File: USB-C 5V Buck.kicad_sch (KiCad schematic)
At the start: 10 parts, among them U8 TPSM365R3RDNR

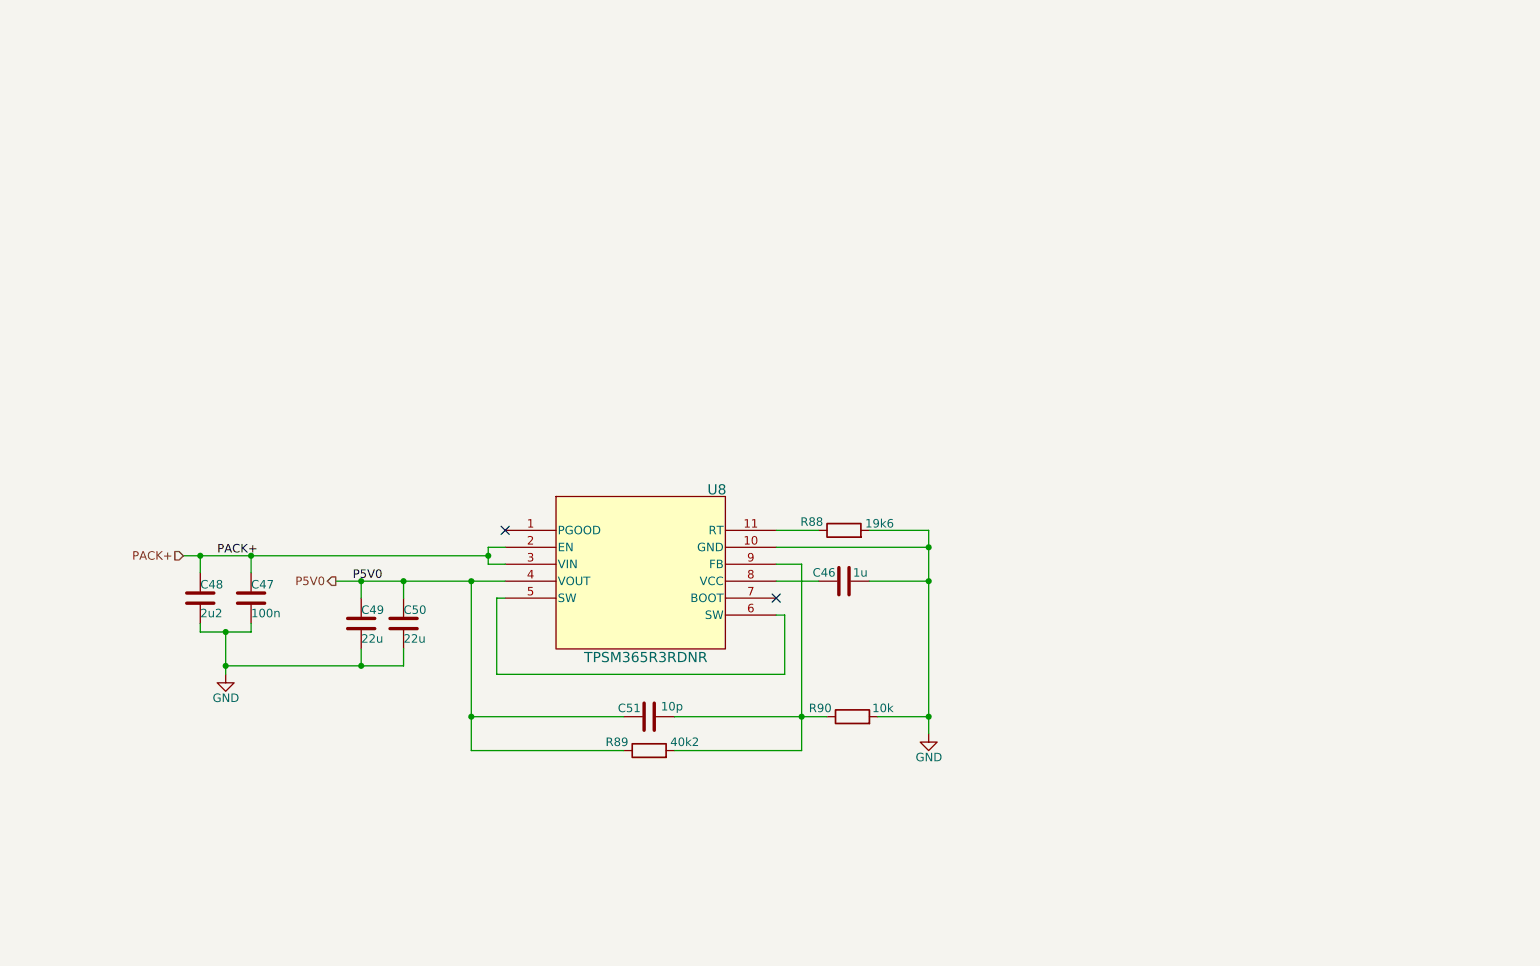
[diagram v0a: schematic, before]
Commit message: Fixed 5V Line
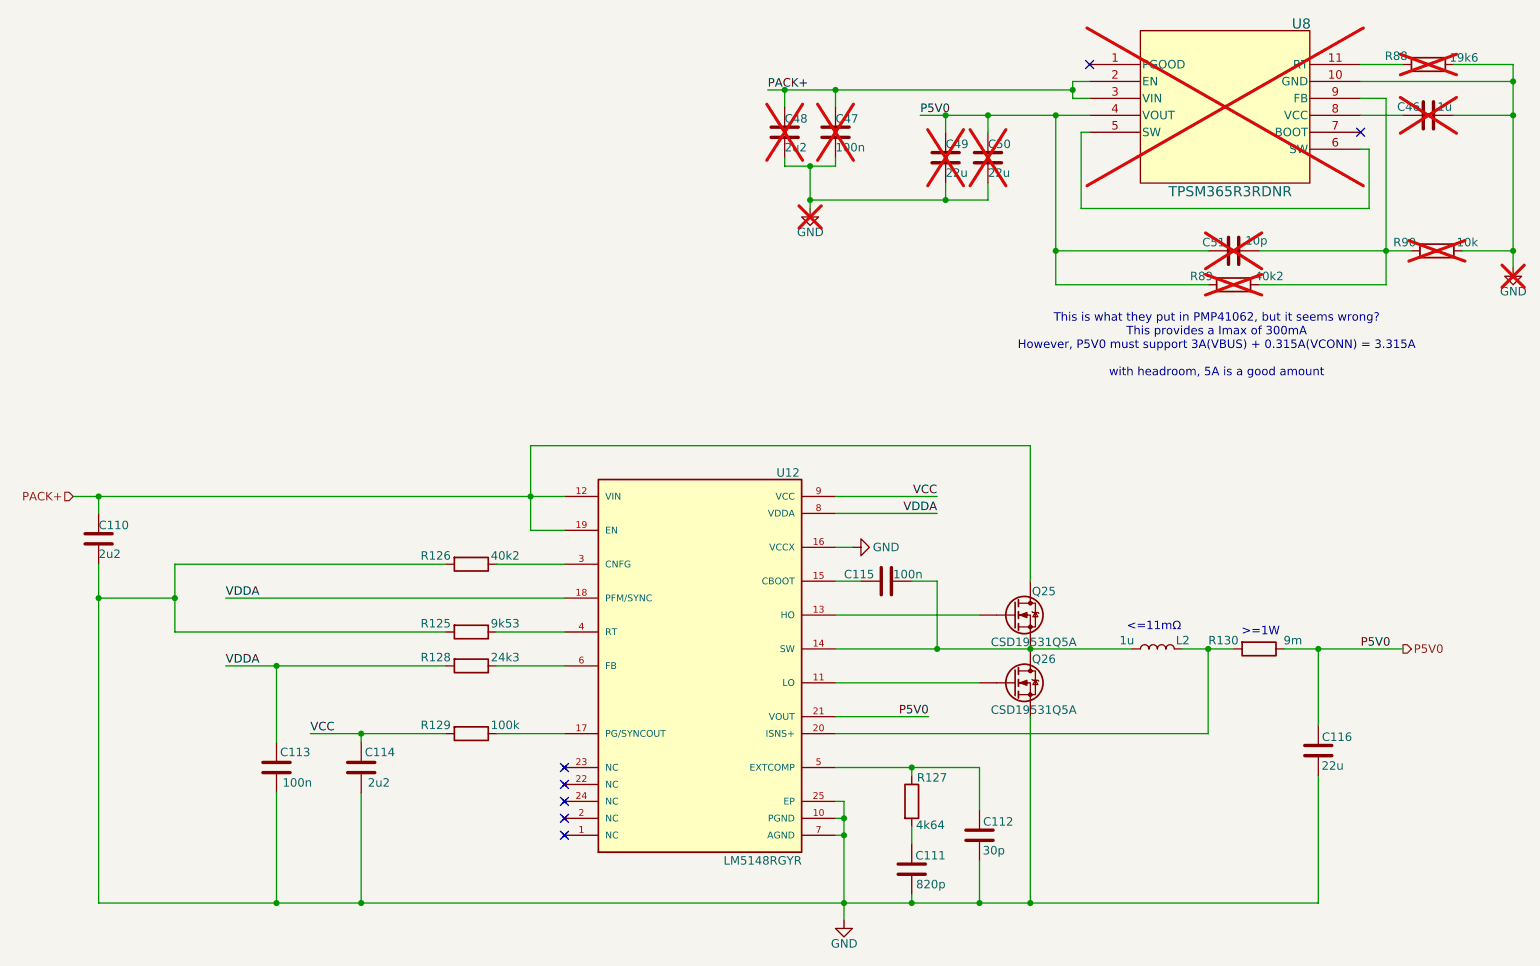
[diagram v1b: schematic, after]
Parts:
- added C110, C114: 2u2, symbol Device:C
- added C111: 820p, symbol Device:C
- added C112: 30p, symbol Device:C
- added C113, C115: 100n, symbol Device:C
- added C116: 22u, symbol Device:C
- added L2: 1u, symbol Device:L
- added Q25, Q26: CSD19531Q5A, Package_TO_SOT_SMD:TDSON-8-1, symbol Transistor_FET:CSD19531Q5A
- added R125: 9k53, symbol Device:R
- added R126: 40k2, symbol Device:R
- added R127: 4k64, symbol Device:R
- added R128: 24k3, symbol Device:R
- added R129: 100k, symbol Device:R
- added R130: 9m, symbol Device:R
- added U12: LM5148RGYR, LM5148RGYR:QFN50P550X350X100-25N, symbol LM5148RGYR:LM5148RGYR
- C46, C47, C48, C49, C50, C51, R88, R89, R90, U8: now not fitted; now left out of the parts list
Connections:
- net GND: now also C110.2, C111.1, C112.1, C113.2, C114.2, C116.1, Q26.1 (S), Q26.2 (S), Q26.3 (S), R125.2, R126.2, U12.10 (PGND), U12.16 (VCCX), U12.25 (EP), U12.7 (AGND)
- net P5V0: now also C116.2, R130.1, U12.21 (VOUT)
- net PACK+: now also C110.1, Q25.5 (D), U12.12 (VIN), U12.19 (EN)
- new net: R129.1, U12.17 (PG/SYNCOUT)
- new net: C115.1, L2.1, Q25.1 (S), Q25.2 (S), Q25.3 (S), Q26.5 (D), U12.14 (SW)
- new net: C115.2, U12.15 (CBOOT)
- new net: Q26.4 (G), U12.11 (LO)
- new net: Q25.4 (G), U12.13 (HO)
- new net: L2.2, R130.2, U12.20 (ISNS+)
- new net: R126.1, U12.3 (CNFG)
- new net: R125.1, U12.4 (RT)
- new net: C112.2, R127.1, U12.5 (EXTCOMP)
- new net: R128.1, U12.6 (FB)
- new net: C111.2, R127.2
- new net VCC: C114.1, R129.2, U12.9 (VCC)
- new net VDDA: C113.1, R128.2, U12.18 (PFM/SYNC), U12.8 (VDDA)
- no-connect marks 2 -> 7
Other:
- note added: "<=11mΩ"
- note added: ">=1W"
- note added: "This is what they put in PMP41062, but it seems wrong? This provides a Imax of 300mA However, P5V0 must support 3A(VBUS) + 0.315A(VCONN) = 3.315A with headroom, 5A is a good amount"
